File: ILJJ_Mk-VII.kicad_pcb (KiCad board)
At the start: 2 copper layers, 48.3 x 99.1 mm, 27 parts, among them J1 Conn_02x12, U1 74LS00, U10 74LS00, U11 74LS00, U2 74LS00, U3 74LS00, U4 74LS00, U5 74LS00, U6 74LS00, U7 74LS00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

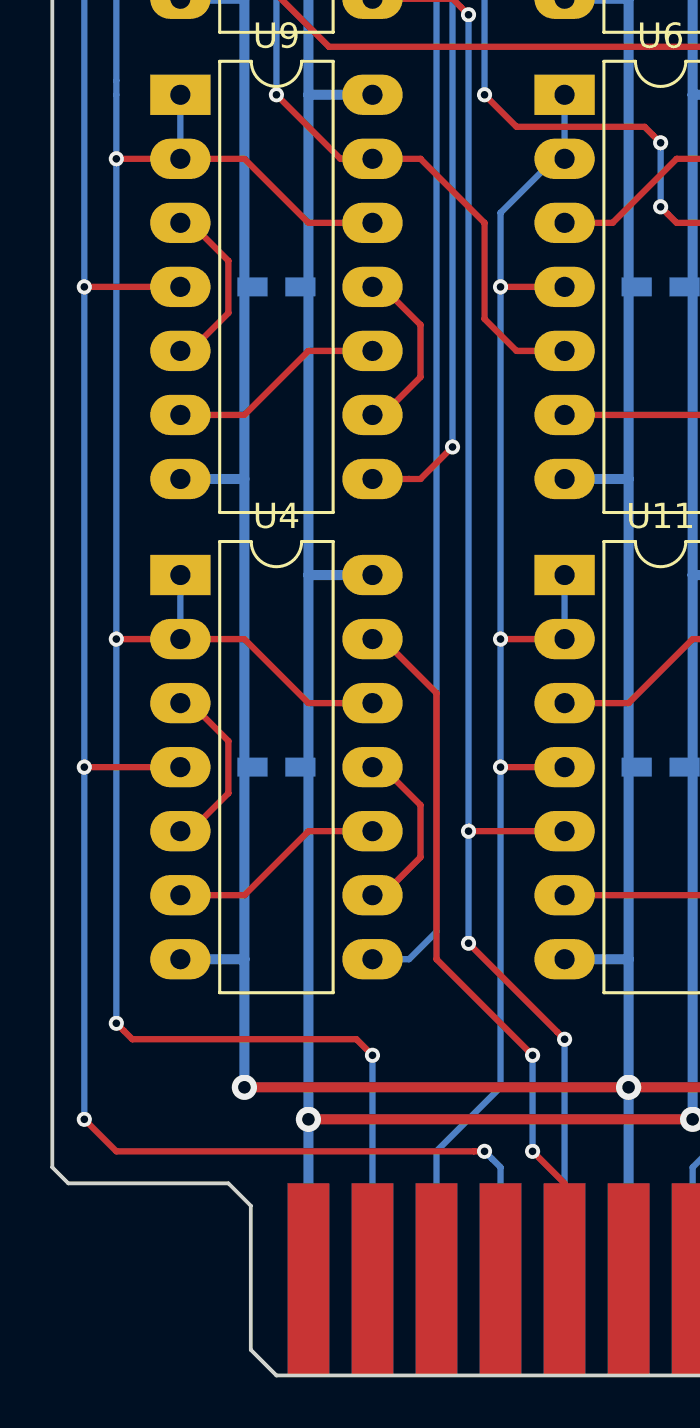
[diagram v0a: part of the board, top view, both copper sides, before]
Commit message: [clean] 配線の微調整
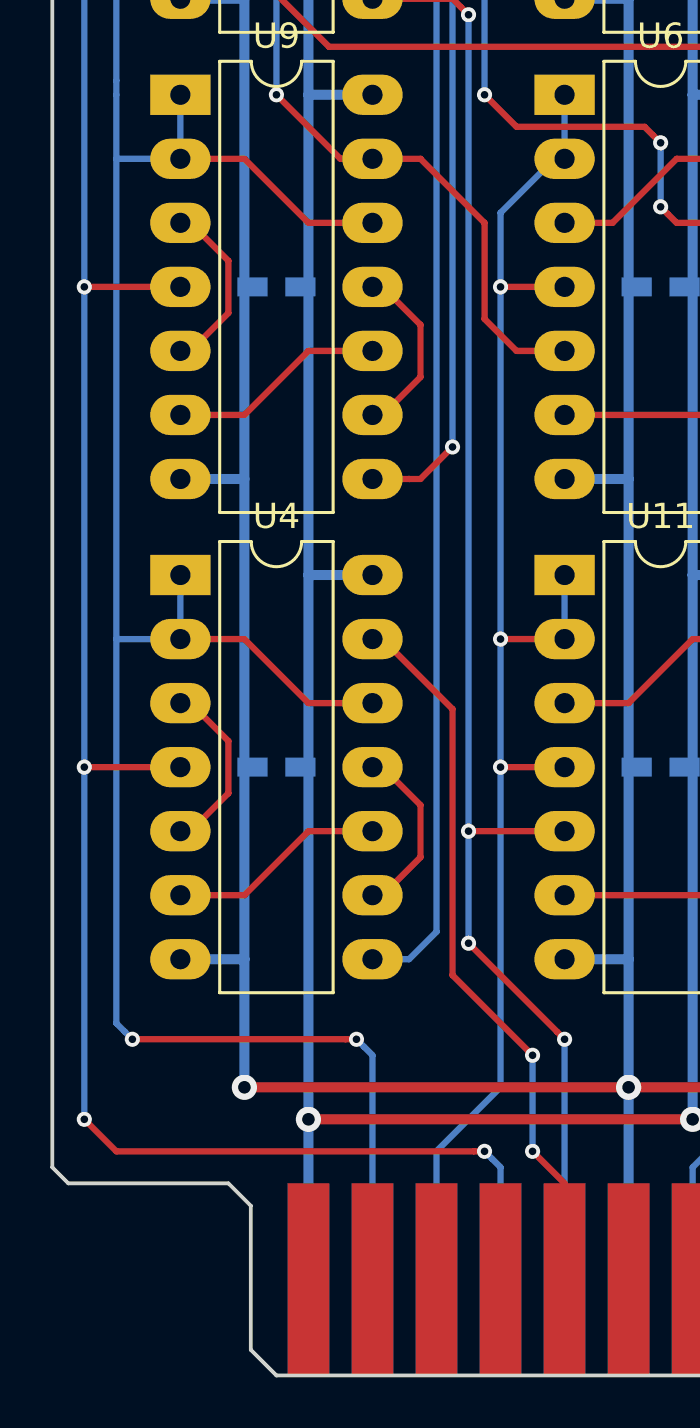
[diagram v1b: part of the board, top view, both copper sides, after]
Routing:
- net /F2: vias 4 -> 2
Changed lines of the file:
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@@
     (thickness 1.6)
     (drawings 16)
-    (tracks 453)
+    (tracks 454)
     (zones 0)
     (modules 27)
@@
   (segment (start 104.14 82.15) (end 104.14 98.494315) (width 0.25) (layer B.Cu) (net 4))
   (segment (start 106.68 80.01) (end 106.28 80.01) (width 0.25) (layer B.Cu) (net 4))
-  (via (at 104.14 101.6) (size 0.6) (drill 0.3) (layers F.Cu B.Cu) (net 4))
   (segment (start 104.14 101.6) (end 104.14 99.06) (width 0.25) (layer B.Cu) (net 4))
-  (segment (start 106.68 101.6) (end 104.14 101.6) (width 0.25) (layer F.Cu) (net 4))
-  (via (at 104.14 120.65) (size 0.6) (drill 0.3) (layers F.Cu B.Cu) (net 4))
-  (segment (start 106.68 120.65) (end 104.14 120.65) (width 0.25) (layer F.Cu) (net 4))
-  (via (at 114.3 137.16) (size 0.6) (drill 0.3) (layers F.Cu B.Cu) (net 4))
-  (segment (start 114.3 146.05) (end 114.3 137.16) (width 0.25) (layer B.Cu) (net 4))
-  (via (at 104.14 135.89) (size 0.6) (drill 0.3) (layers F.Cu B.Cu) (net 4))
-  (segment (start 104.14 101.6) (end 104.14 135.89) (width 0.25) (layer B.Cu) (net 4))
-  (segment (start 104.775 136.525) (end 104.439999 136.189999) (width 0.25) (layer F.Cu) (net 4))
-  (segment (start 104.439999 136.189999) (end 104.14 135.89) (width 0.25) (layer F.Cu) (net 4))
-  (segment (start 113.665 136.525) (end 104.775 136.525) (width 0.25) (layer F.Cu) (net 4))
-  (segment (start 114.3 137.16) (end 113.665 136.525) (width 0.25) (layer F.Cu) (net 4))
+  (via (at 113.664988 136.525) (size 0.6) (drill 0.3) (layers F.Cu B.Cu) (net 4))
+  (segment (start 114.3 146.05) (end 114.3 137.160012) (width 0.25) (layer B.Cu) (net 4))
+  (segment (start 114.3 137.160012) (end 113.964987 136.824999) (width 0.25) (layer B.Cu) (net 4))
+  (segment (start 113.964987 136.824999) (end 113.664988 136.525) (width 0.25) (layer B.Cu) (net 4))
+  (segment (start 104.475017 136.225001) (end 104.775016 136.525) (width 0.25) (layer B.Cu) (net 4))
+  (segment (start 113.240724 136.525) (end 104.775016 136.525) (width 0.25) (layer F.Cu) (net 4))
+  (via (at 104.775016 136.525) (size 0.6) (drill 0.3) (layers F.Cu B.Cu) (net 4))
+  (segment (start 113.664988 136.525) (end 113.240724 136.525) (width 0.25) (layer F.Cu) (net 4))
+  (segment (start 104.14 135.889984) (end 104.475017 136.225001) (width 0.25) (layer B.Cu) (net 4))
+  (segment (start 106.68 120.65) (end 104.14 120.65) (width 0.25) (layer B.Cu) (net 4))
+  (segment (start 104.14 120.65) (end 104.14 135.889984) (width 0.25) (layer B.Cu) (net 4))
+  (segment (start 104.14 101.6) (end 104.14 120.65) (width 0.25) (layer B.Cu) (net 4))
+  (segment (start 106.68 101.6) (end 104.14 101.6) (width 0.25) (layer B.Cu) (net 4))
   (segment (start 116.84 146.05) (end 116.84 140.97) (width 0.25) (layer B.Cu) (net 5))
   (segment (start 116.84 140.97) (end 119.38 138.43) (width 0.25) (layer B.Cu) (net 5))
@@
   (segment (start 114.3 120.65) (end 114.7 120.65) (width 0.25) (layer B.Cu) (net 7))
   (segment (start 114.7 120.65) (end 114.3 120.65) (width 0.25) (layer F.Cu) (net 7))
-  (segment (start 116.84 122.79) (end 114.7 120.65) (width 0.25) (layer F.Cu) (net 7))
-  (segment (start 116.84 133.35) (end 116.84 122.79) (width 0.25) (layer F.Cu) (net 7))
-  (segment (start 120.65 137.16) (end 116.84 133.35) (width 0.25) (layer F.Cu) (net 7))
+  (segment (start 117.475 123.425) (end 114.7 120.65) (width 0.25) (layer F.Cu) (net 7))
+  (segment (start 117.475 133.985) (end 117.475 123.425) (width 0.25) (layer F.Cu) (net 7))
+  (segment (start 120.65 137.16) (end 117.475 133.985) (width 0.25) (layer F.Cu) (net 7))
   (segment (start 121.92 128.27) (end 118.11 128.27) (width 0.25) (layer F.Cu) (net 8))
   (via (at 118.11 128.27) (size 0.6) (drill 0.3) (layers F.Cu B.Cu) (net 8))

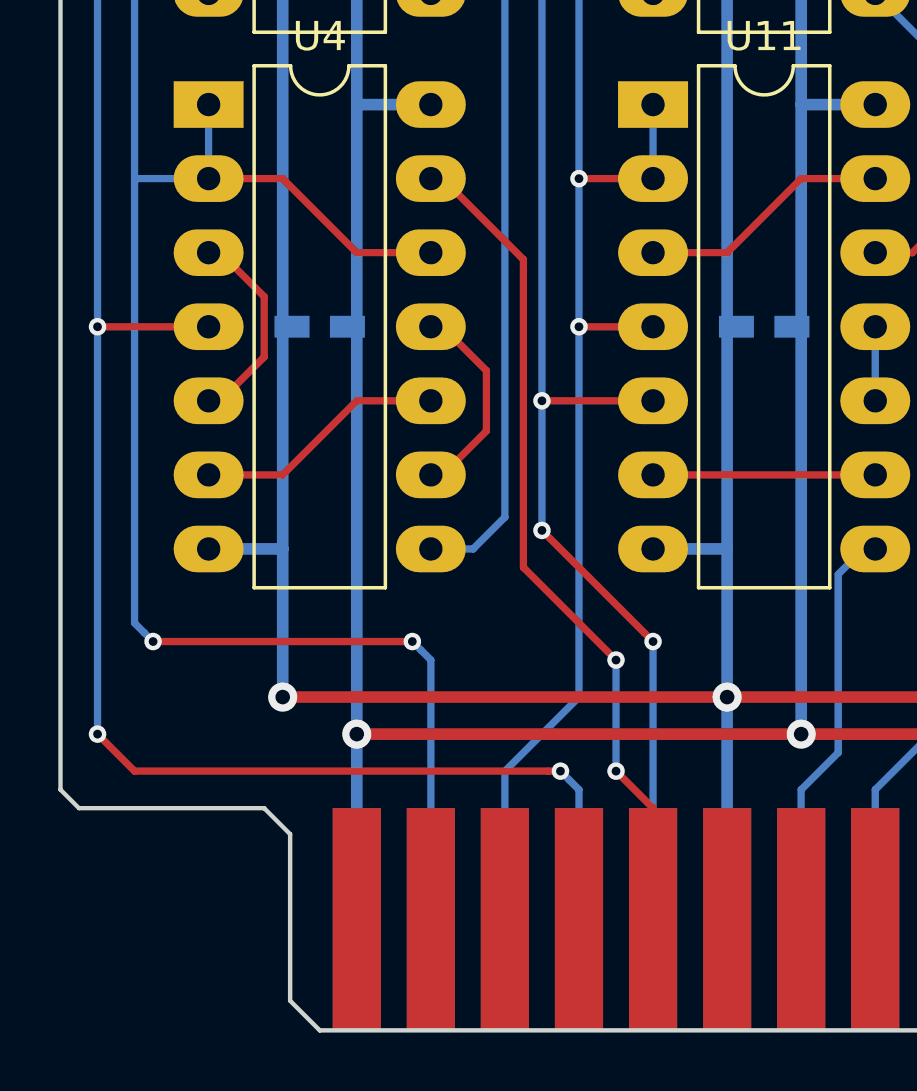
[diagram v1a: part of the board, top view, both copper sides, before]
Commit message: [fix] コネクタの両側短絡すべきポートが短絡していないのを修正
この方法で合ってるのか不安
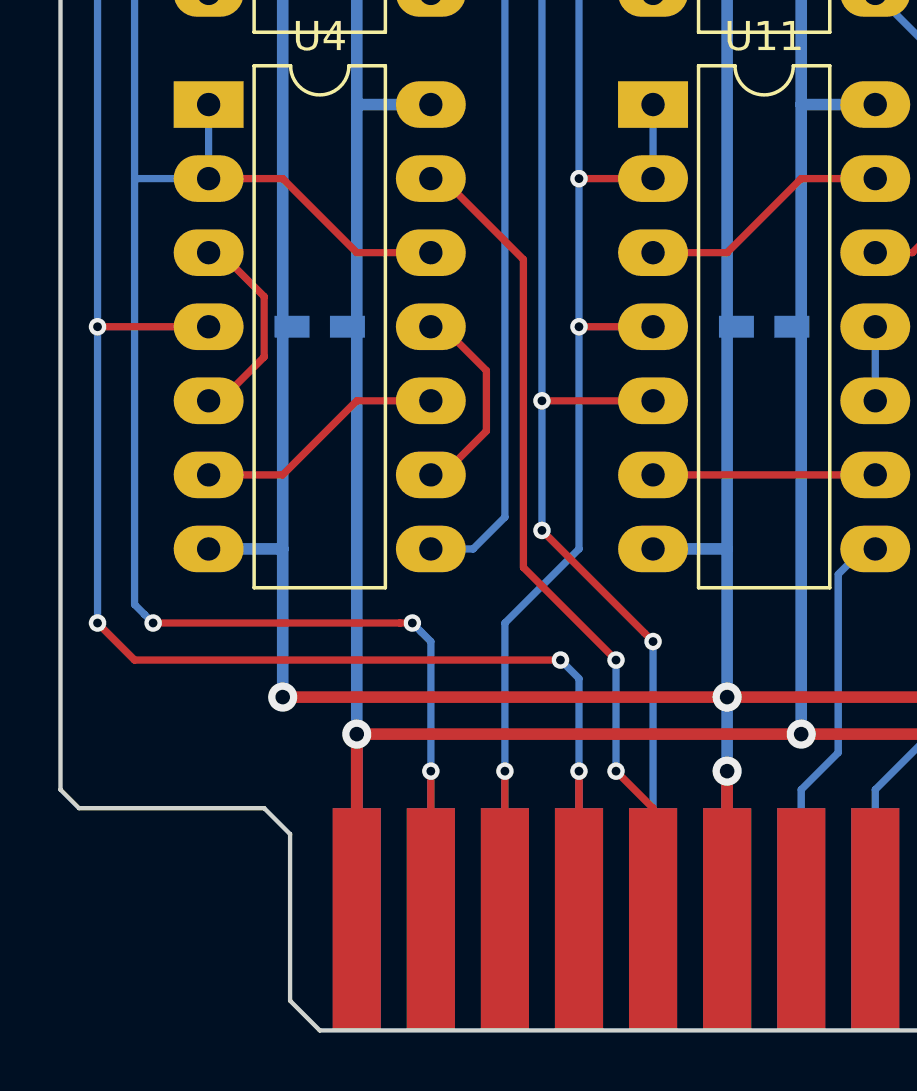
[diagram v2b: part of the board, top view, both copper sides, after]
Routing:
- net VCC: track 289.8 -> 296.2 mm
- net /F2: track 104.2 -> 109.3 mm, vias 2 -> 3
- net GND: track 273.5 -> 278.6 mm, vias 3 -> 4
- net /F1: track 59.5 -> 64.6 mm, vias 3 -> 4
- net /F0: track 89.6 -> 94.7 mm, vias 5 -> 6
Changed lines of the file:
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@@
     (thickness 1.6)
     (drawings 16)
-    (tracks 454)
+    (tracks 463)
     (zones 0)
     (modules 27)
@@
   (via (at 124.46 138.43) (size 1) (drill 0.5) (layers F.Cu B.Cu) (net 1))
   (segment (start 124.46 133.35) (end 124.46 138.43) (width 0.4) (layer B.Cu) (net 1))
-  (segment (start 124.46 138.43) (end 124.46 146.05) (width 0.4) (layer B.Cu) (net 1))
   (via (at 109.22 138.43) (size 1) (drill 0.5) (layers F.Cu B.Cu) (net 1))
   (segment (start 124.46 138.43) (end 109.22 138.43) (width 0.4) (layer F.Cu) (net 1))
@@
   (segment (start 139.7 133.35) (end 139.7 135.255) (width 0.4) (layer B.Cu) (net 1))
   (segment (start 139.7 135.255) (end 137.024999 137.930001) (width 0.4) (layer B.Cu) (net 1))
+  (segment (start 124.46 140.97) (end 124.46 146.05) (width 0.4) (layer B.Cu) (net 1))
+  (via (at 124.46 140.97) (size 1) (drill 0.5) (layers F.Cu B.Cu) (net 1))
+  (segment (start 124.46 146.05) (end 124.46 140.97) (width 0.4) (layer F.Cu) (net 1))
+  (segment (start 124.46 138.43) (end 124.46 140.97) (width 0.4) (layer B.Cu) (net 1))
   (segment (start 114.3 60.96) (end 111.76 60.96) (width 0.4) (layer B.Cu) (net 2))
   (segment (start 111.76 118.11) (end 114.3 118.11) (width 0.4) (layer B.Cu) (net 2))
@@
   (segment (start 137.756838 139.7) (end 137.775919 139.680919) (width 0.4) (layer F.Cu) (net 2))
   (segment (start 142.24 135.216838) (end 138.275918 139.18092) (width 0.4) (layer B.Cu) (net 2))
+  (segment (start 111.76 146.05) (end 111.76 139.7) (width 0.4) (layer F.Cu) (net 2))
   (segment (start 119.38 53.975) (end 114.935 53.975) (width 0.25) (layer F.Cu) (net 3))
   (segment (start 106.68 120.65) (end 109.22 120.65) (width 0.25) (layer F.Cu) (net 4))
@@
   (segment (start 106.68 80.01) (end 106.28 80.01) (width 0.25) (layer B.Cu) (net 4))
   (segment (start 104.14 101.6) (end 104.14 99.06) (width 0.25) (layer B.Cu) (net 4))
-  (via (at 113.664988 136.525) (size 0.6) (drill 0.3) (layers F.Cu B.Cu) (net 4))
-  (segment (start 114.3 146.05) (end 114.3 137.160012) (width 0.25) (layer B.Cu) (net 4))
-  (segment (start 114.3 137.160012) (end 113.964987 136.824999) (width 0.25) (layer B.Cu) (net 4))
-  (segment (start 113.964987 136.824999) (end 113.664988 136.525) (width 0.25) (layer B.Cu) (net 4))
-  (segment (start 104.475017 136.225001) (end 104.775016 136.525) (width 0.25) (layer B.Cu) (net 4))
-  (segment (start 113.240724 136.525) (end 104.775016 136.525) (width 0.25) (layer F.Cu) (net 4))
-  (via (at 104.775016 136.525) (size 0.6) (drill 0.3) (layers F.Cu B.Cu) (net 4))
-  (segment (start 113.664988 136.525) (end 113.240724 136.525) (width 0.25) (layer F.Cu) (net 4))
-  (segment (start 104.14 135.889984) (end 104.475017 136.225001) (width 0.25) (layer B.Cu) (net 4))
   (segment (start 106.68 120.65) (end 104.14 120.65) (width 0.25) (layer B.Cu) (net 4))
-  (segment (start 104.14 120.65) (end 104.14 135.889984) (width 0.25) (layer B.Cu) (net 4))
   (segment (start 104.14 101.6) (end 104.14 120.65) (width 0.25) (layer B.Cu) (net 4))
   (segment (start 106.68 101.6) (end 104.14 101.6) (width 0.25) (layer B.Cu) (net 4))
-  (segment (start 116.84 146.05) (end 116.84 140.97) (width 0.25) (layer B.Cu) (net 5))
-  (segment (start 116.84 140.97) (end 119.38 138.43) (width 0.25) (layer B.Cu) (net 5))
+  (via (at 113.665 135.89) (size 0.6) (drill 0.3) (layers F.Cu B.Cu) (net 4))
+  (segment (start 114.3 136.525) (end 113.964999 136.189999) (width 0.25) (layer B.Cu) (net 4))
+  (segment (start 113.964999 136.189999) (end 113.665 135.89) (width 0.25) (layer B.Cu) (net 4))
+  (segment (start 113.665 135.89) (end 113.240736 135.89) (width 0.25) (layer F.Cu) (net 4))
+  (segment (start 104.14 120.65) (end 104.14 135.255) (width 0.25) (layer B.Cu) (net 4))
+  (via (at 104.775 135.89) (size 0.6) (drill 0.3) (layers F.Cu B.Cu) (net 4))
+  (segment (start 113.240736 135.89) (end 104.775 135.89) (width 0.25) (layer F.Cu) (net 4))
+  (segment (start 104.475001 135.590001) (end 104.775 135.89) (width 0.25) (layer B.Cu) (net 4))
+  (segment (start 104.14 135.255) (end 104.475001 135.590001) (width 0.25) (layer B.Cu) (net 4))
+  (via (at 114.3 140.97) (size 0.6) (drill 0.3) (layers F.Cu B.Cu) (net 4))
+  (segment (start 114.3 146.05) (end 114.3 140.97) (width 0.25) (layer F.Cu) (net 4))
+  (segment (start 114.3 140.97) (end 114.3 136.525) (width 0.25) (layer B.Cu) (net 4))
+  (segment (start 114.3 146.05) (end 114.3 140.97) (width 0.25) (layer B.Cu) (net 4))
   (segment (start 119.38 103.74) (end 121.52 101.6) (width 0.25) (layer B.Cu) (net 5))
   (segment (start 121.52 101.6) (end 121.92 101.6) (width 0.25) (layer B.Cu) (net 5))
@@
   (segment (start 121.92 125.73) (end 119.38 125.73) (width 0.25) (layer F.Cu) (net 5))
   (segment (start 119.38 125.73) (end 119.38 120.65) (width 0.25) (layer B.Cu) (net 5))
-  (segment (start 119.38 138.43) (end 119.38 125.73) (width 0.25) (layer B.Cu) (net 5))
-  (via (at 102.87 139.7) (size 0.6) (drill 0.3) (layers F.Cu B.Cu) (net 6))
+  (segment (start 116.84 135.89) (end 119.38 133.35) (width 0.25) (layer B.Cu) (net 5))
+  (segment (start 119.38 133.35) (end 119.38 125.73) (width 0.25) (layer B.Cu) (net 5))
+  (segment (start 116.84 146.05) (end 116.84 135.89) (width 0.25) (layer B.Cu) (net 5))
+  (via (at 116.84 140.97) (size 0.6) (drill 0.3) (layers F.Cu B.Cu) (net 5))
+  (segment (start 116.84 146.05) (end 116.84 140.97) (width 0.25) (layer F.Cu) (net 5))
   (via (at 102.87 83.82) (size 0.6) (drill 0.3) (layers F.Cu B.Cu) (net 6))
   (segment (start 104.14 82.55) (end 102.87 83.82) (width 0.25) (layer F.Cu) (net 6))
@@
   (segment (start 106.68 125.73) (end 102.87 125.73) (width 0.25) (layer F.Cu) (net 6))
   (segment (start 102.87 125.73) (end 102.87 106.68) (width 0.25) (layer B.Cu) (net 6))
-  (segment (start 102.87 139.7) (end 102.87 125.73) (width 0.25) (layer B.Cu) (net 6))
-  (via (at 118.745 140.97) (size 0.6) (drill 0.3) (layers F.Cu B.Cu) (net 6))
-  (segment (start 119.38 141.605) (end 119.044999 141.269999) (width 0.25) (layer B.Cu) (net 6))
-  (segment (start 119.044999 141.269999) (end 118.745 140.97) (width 0.25) (layer B.Cu) (net 6))
-  (segment (start 102.87 139.7) (end 104.14 140.97) (width 0.25) (layer F.Cu) (net 6))
-  (segment (start 104.14 140.97) (end 118.320736 140.97) (width 0.25) (layer F.Cu) (net 6))
-  (segment (start 119.38 146.05) (end 119.38 141.605) (width 0.25) (layer B.Cu) (net 6))
-  (segment (start 118.320736 140.97) (end 118.745 140.97) (width 0.25) (layer F.Cu) (net 6))
+  (segment (start 119.38 137.795) (end 118.745 137.16) (width 0.25) (layer B.Cu) (net 6))
+  (segment (start 119.38 146.05) (end 119.38 137.795) (width 0.25) (layer B.Cu) (net 6))
+  (segment (start 102.87 125.73) (end 102.87 135.89) (width 0.25) (layer B.Cu) (net 6))
+  (via (at 102.87 135.89) (size 0.6) (drill 0.3) (layers F.Cu B.Cu) (net 6))
+  (via (at 118.745 137.16) (size 0.6) (drill 0.3) (layers F.Cu B.Cu) (net 6))
+  (segment (start 104.14 137.16) (end 102.87 135.89) (width 0.25) (layer F.Cu) (net 6))
+  (segment (start 118.745 137.16) (end 104.14 137.16) (width 0.25) (layer F.Cu) (net 6))
+  (via (at 119.38 140.97) (size 0.6) (drill 0.3) (layers F.Cu B.Cu) (net 6))
+  (segment (start 119.38 146.05) (end 119.38 140.97) (width 0.25) (layer F.Cu) (net 6))
   (segment (start 121.92 146.05) (end 121.92 143.0655) (width 0.25) (layer F.Cu) (net 7))
   (segment (start 121.92 142.24) (end 120.65 140.97) (width 0.25) (layer F.Cu) (net 7))

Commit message: [add] some logos
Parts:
- added G***: LOGO, fplib:designed-in-ILJJ, F.Cu at (140.3, 67.9)
- added REF***: KiCad-Logo2_6mm_SilkScreen, Symbols:KiCad-Logo2_6mm_SilkScreen, F.Cu at (135.9, 54.4)
